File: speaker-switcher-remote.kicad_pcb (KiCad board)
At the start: 2 copper layers, 91 x 60 mm, 30 parts, among them M1 arduino-nano, Q1 2N2222, Q2 TIP31C, U1 LM7805_TO220

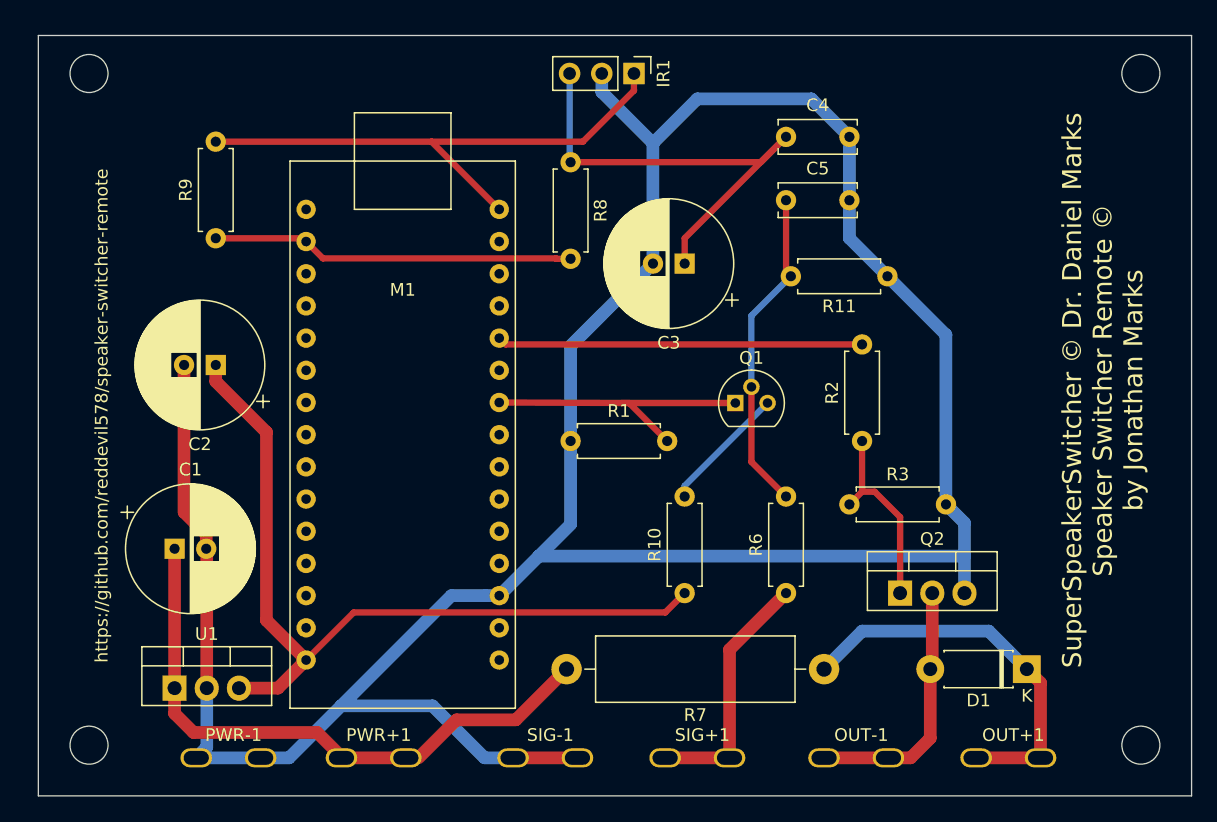
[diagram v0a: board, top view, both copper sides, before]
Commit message: Elongated board to required mounting width
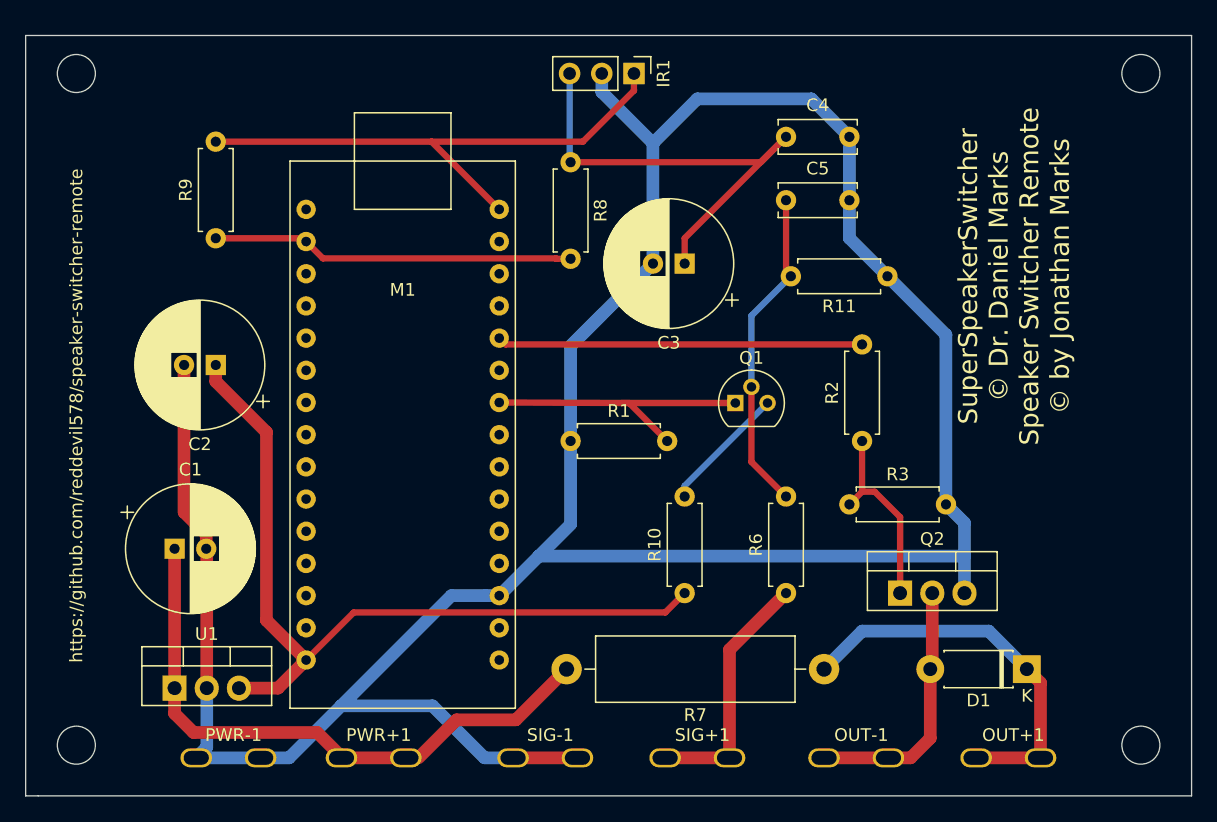
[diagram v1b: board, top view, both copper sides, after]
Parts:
- moved REF** 1.00 mm to (106.2, 71.5)
- moved REF** 1.00 mm to (106.2, 124.5)
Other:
- board size 91 x 60 mm -> 92 x 60 mm
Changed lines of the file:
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@@
   (general
     (thickness 1.6)
-    (drawings 6)
+    (drawings 7)
     (tracks 114)
     (zones 0)
@@
   )
   (module MountingHole:MountingHole_3mm (layer F.Cu)
-    (at 107.25 71.5)
+    (at 106.25 71.5)
     (descr "Mounting Hole 3mm, no annular")
     (tags "mounting hole 3mm no annular")
@@
   )
   (module MountingHole:MountingHole_3mm (layer F.Cu)
-    (at 107.25 124.5)
+    (at 106.25 124.5)
     (descr "Mounting Hole 3mm, no annular")
     (tags "mounting hole 3mm no annular")
@@
     )
   )
-  (gr_text https://github.com/reddevil578/speaker-switcher-remote (at 108.25 98.5 90) (layer F.SilkS)
+  (gr_line (start 102.25 68.5) (end 194.25 68.5) (layer Edge.Cuts) (width 0.05))
+  (gr_line (start 102.25 128.5) (end 103.25 128.5) (layer Edge.Cuts) (width 0.05))
+  (gr_text https://github.com/reddevil578/speaker-switcher-remote (at 106.25 98.5 90) (layer F.SilkS)
     (effects (font (size 1 1) (thickness 0.25)))
   )
-  (gr_text "SuperSpeakerSwitcher © Dr. Daniel Marks\nSpeaker Switcher Remote ©\nby Jonathan Marks" (at 187.25 96.5 90) (layer F.SilkS)
+  (gr_text "SuperSpeakerSwitcher\n© Dr. Daniel Marks\nSpeaker Switcher Remote\n© by Jonathan Marks" (at 180.25 87.5 90) (layer F.SilkS)
     (effects (font (size 1.5 1.5) (thickness 0.3)))
   )
-  (gr_line (start 103.25 128.5) (end 103.25 68.5) (layer Edge.Cuts) (width 0.05))
+  (gr_line (start 102.25 128.5) (end 102.25 68.5) (layer Edge.Cuts) (width 0.05))
   (gr_line (start 194.25 128.5) (end 103.25 128.5) (layer Edge.Cuts) (width 0.05))
   (gr_line (start 194.25 68.5) (end 194.25 128.5) (layer Edge.Cuts) (width 0.05))
-  (gr_line (start 103.25 68.5) (end 194.25 68.5) (layer Edge.Cuts) (width 0.05))
   (segment (start 116.33 120.21) (end 116.54 120) (width 1) (layer F.Cu) (net 1) (status 30))
   (segment (start 116.54 109.04) (end 116.5 109) (width 1) (layer F.Cu) (net 1) (status 30))
@@
   (segment (start 116.5 109) (end 116.5 107.86863) (width 1) (layer F.Cu) (net 1) (status 10))
   (segment (start 140.71 125.5) (end 145.79 125.5) (width 1) (layer F.Cu) (net 1) (status 30))
-  (segment (start 134.28 76.88) (end 139.62 82.22) (width 0.5) (layer F.Cu) (net 2) (status 20))
-  (segment (start 117.25 76.88) (end 134.28 76.88) (width 0.5) (layer F.Cu) (net 2) (status 10))
-  (segment (start 158.25 97.5) (end 149.25 97.5) (width 0.5) (layer F.Cu) (net 10) (status 10))
-  (segment (start 149.25 97.5) (end 139.62 97.46) (width 0.5) (layer F.Cu) (net 10) (status 20))
-  (segment (start 140.12 92.88) (end 139.62 92.38) (width 0.5) (layer F.Cu) (net 12) (status 30))
-  (segment (start 168.25 92.88) (end 140.12 92.88) (width 0.5) (layer F.Cu) (net 12) (status 30))
-  (segment (start 152.71 125.5) (end 157.79 125.5) (width 1) (layer F.Cu) (net 30) (status 30))
-  (segment (start 117.25 95.8) (end 121.25 99.8) (width 1) (layer F.Cu) (net 31))
-  (segment (start 117.25 94.5) (end 117.25 95.8) (width 1) (layer F.Cu) (net 31) (status 10))
-  (segment (start 121.25 114.65) (end 124.38 117.78) (width 1) (layer F.Cu) (net 31) (status 20))
-  (segment (start 121.25 99.8) (end 121.25 114.65) (width 1) (layer F.Cu) (net 31))
-  (segment (start 122.16 120) (end 124.38 117.78) (width 1) (layer F.Cu) (net 31) (status 20))
-  (segment (start 119.08 120) (end 122.16 120) (width 1) (layer F.Cu) (net 31) (status 10))
-  (segment (start 152.722001 114.027999) (end 154.25 112.5) (width 0.5) (layer F.Cu) (net 31) (status 20))
-  (segment (start 128.132001 114.027999) (end 152.722001 114.027999) (width 0.5) (layer F.Cu) (net 31))
-  (segment (start 124.38 117.78) (end 128.132001 114.027999) (width 0.5) (layer F.Cu) (net 31) (status 10))
-  (segment (start 114 109) (end 114 120) (width 1) (layer F.Cu) (net 32) (status 30))
-  (segment (start 114 120.0475) (end 114 120) (width 1) (layer B.Cu) (net 32) (status 30))
-  (segment (start 114 120) (end 114 120.0475) (width 1) (layer F.Cu) (net 32) (status 30))
-  (segment (start 133.25 125.5) (end 136.25 122.5) (width 1) (layer F.Cu) (net 32))
-  (segment (start 140.93 122.5) (end 144.93 118.5) (width 1) (layer F.Cu) (net 32) (status 20))
-  (segment (start 136.25 122.5) (end 140.93 122.5) (width 1) (layer F.Cu) (net 32))
   (segment (start 176.33 112.5) (end 176.33 112.5475) (width 1) (layer B.Cu) (net 1) (status 30))
   (segment (start 145.25 93) (end 151.75 86.5) (width 1) (layer B.Cu) (net 1) (status 20))
@@
   (segment (start 123.04 125.5) (end 127.145 121.395) (width 1) (layer B.Cu) (net 1))
   (segment (start 127.145 121.395) (end 135.84 112.7) (width 1) (layer B.Cu) (net 1))
+  (segment (start 134.28 76.88) (end 139.62 82.22) (width 0.5) (layer F.Cu) (net 2) (status 20))
+  (segment (start 117.25 76.88) (end 134.28 76.88) (width 0.5) (layer F.Cu) (net 2) (status 10))
+  (segment (start 150.25 71.5) (end 150.33 71.5) (width 0.5) (layer F.Cu) (net 2) (status 30))
+  (segment (start 150.25 71.5) (end 150.25 71.032002) (width 0.5) (layer F.Cu) (net 2))
+  (segment (start 150.25 72.85) (end 150.25 71.5) (width 0.5) (layer F.Cu) (net 2))
+  (segment (start 146.22 76.88) (end 150.25 72.85) (width 0.5) (layer F.Cu) (net 2))
+  (segment (start 134.28 76.88) (end 146.22 76.88) (width 0.5) (layer F.Cu) (net 2))
+  (segment (start 158.25 97.5) (end 149.25 97.5) (width 0.5) (layer F.Cu) (net 10) (status 10))
+  (segment (start 149.25 97.5) (end 139.62 97.46) (width 0.5) (layer F.Cu) (net 10) (status 20))
   (segment (start 149.87 97.5) (end 149.25 97.5) (width 0.5) (layer F.Cu) (net 10))
   (segment (start 152.87 100.5) (end 149.87 97.5) (width 0.5) (layer F.Cu) (net 10) (status 10))
+  (segment (start 140.12 92.88) (end 139.62 92.38) (width 0.5) (layer F.Cu) (net 12) (status 30))
+  (segment (start 168.25 92.88) (end 140.12 92.88) (width 0.5) (layer F.Cu) (net 12) (status 30))
   (segment (start 168.25 104.5) (end 167.25 105.5) (width 0.5) (layer F.Cu) (net 29) (status 20))
   (segment (start 168.25 100.5) (end 168.25 104.5) (width 0.5) (layer F.Cu) (net 29) (status 10))
@@
   (segment (start 171.25 106.5) (end 171.25 112.5) (width 0.5) (layer F.Cu) (net 29) (status 20))
   (segment (start 169.25 104.5) (end 171.25 106.5) (width 0.5) (layer F.Cu) (net 29))
+  (segment (start 152.71 125.5) (end 157.79 125.5) (width 1) (layer F.Cu) (net 30) (status 30))
   (segment (start 157.79 116.96) (end 157.79 125.5) (width 1) (layer F.Cu) (net 30) (status 20))
   (segment (start 162.25 112.5) (end 157.79 116.96) (width 1) (layer F.Cu) (net 30) (status 10))
-  (segment (start 150.25 71.5) (end 150.33 71.5) (width 0.5) (layer F.Cu) (net 2) (status 30))
-  (segment (start 150.25 71.5) (end 150.25 71.032002) (width 0.5) (layer F.Cu) (net 2))
-  (segment (start 150.25 72.85) (end 150.25 71.5) (width 0.5) (layer F.Cu) (net 2))
-  (segment (start 146.22 76.88) (end 150.25 72.85) (width 0.5) (layer F.Cu) (net 2))
-  (segment (start 134.28 76.88) (end 146.22 76.88) (width 0.5) (layer F.Cu) (net 2))
+  (segment (start 117.25 95.8) (end 121.25 99.8) (width 1) (layer F.Cu) (net 31))
+  (segment (start 117.25 94.5) (end 117.25 95.8) (width 1) (layer F.Cu) (net 31) (status 10))
+  (segment (start 121.25 114.65) (end 124.38 117.78) (width 1) (layer F.Cu) (net 31) (status 20))
+  (segment (start 121.25 99.8) (end 121.25 114.65) (width 1) (layer F.Cu) (net 31))
+  (segment (start 122.16 120) (end 124.38 117.78) (width 1) (layer F.Cu) (net 31) (status 20))
+  (segment (start 119.08 120) (end 122.16 120) (width 1) (layer F.Cu) (net 31) (status 10))
+  (segment (start 152.722001 114.027999) (end 154.25 112.5) (width 0.5) (layer F.Cu) (net 31) (status 20))
+  (segment (start 128.132001 114.027999) (end 152.722001 114.027999) (width 0.5) (layer F.Cu) (net 31))
+  (segment (start 124.38 117.78) (end 128.132001 114.027999) (width 0.5) (layer F.Cu) (net 31) (status 10))
+  (segment (start 114 109) (end 114 120) (width 1) (layer F.Cu) (net 32) (status 30))
+  (segment (start 114 120.0475) (end 114 120) (width 1) (layer B.Cu) (net 32) (status 30))
+  (segment (start 114 120) (end 114 120.0475) (width 1) (layer F.Cu) (net 32) (status 30))
+  (segment (start 133.25 125.5) (end 136.25 122.5) (width 1) (layer F.Cu) (net 32))
+  (segment (start 140.93 122.5) (end 144.93 118.5) (width 1) (layer F.Cu) (net 32) (status 20))
+  (segment (start 136.25 122.5) (end 140.93 122.5) (width 1) (layer F.Cu) (net 32))
   (segment (start 114 122) (end 115.5 123.5) (width 1) (layer F.Cu) (net 32))
   (segment (start 114 120) (end 114 122) (width 1) (layer F.Cu) (net 32))
@@
     (polygon
       (pts
-        (xy 105.25 128.5) (xy 103.25 128.5) (xy 103.25 68.5) (xy 105.25 68.5)
+        (xy 104.25 128.5) (xy 102.25 128.5) (xy 102.25 68.5) (xy 104.25 68.5)
       )
     )

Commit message: Updated board as per Dan's remarks
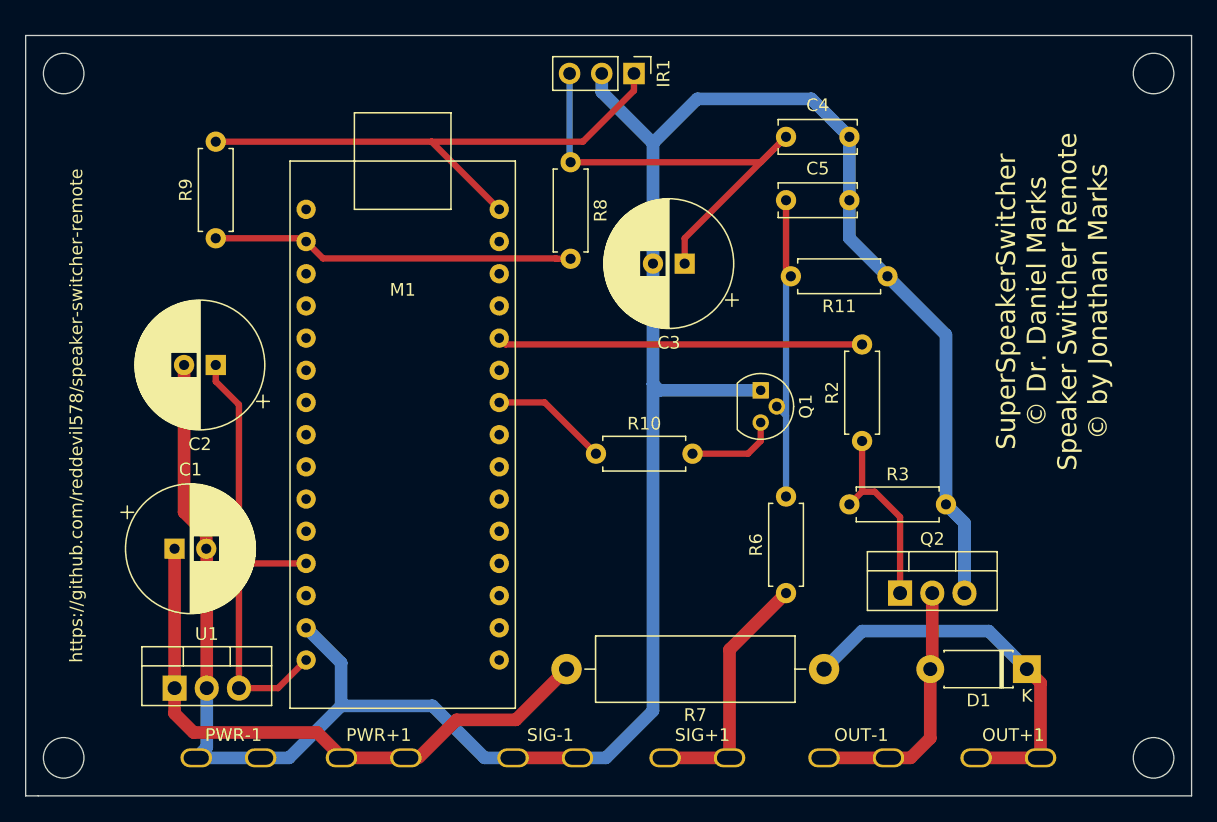
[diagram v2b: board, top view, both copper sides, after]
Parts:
- removed R1: 100k, Resistor_THT:R_Axial_DIN0207_L6.3mm_D2.5mm_P7.62mm_Horizontal
- removed the REF** at (190.2, 71.5)
- removed the REF** at (106.2, 71.5)
- removed the REF** at (106.2, 124.5)
- removed the REF** at (190.2, 124.5)
- added REF**: MountingHole_3.2mm_M3, MountingHole:MountingHole_3.2mm_M3, F.Cu at (105.2, 125.5)
- added REF**: MountingHole_3.2mm_M3, MountingHole:MountingHole_3.2mm_M3, F.Cu at (191.2, 125.5)
- added REF**: MountingHole_3.2mm_M3, MountingHole:MountingHole_3.2mm_M3, F.Cu at (191.2, 71.5)
- added REF**: MountingHole_3.2mm_M3, MountingHole:MountingHole_3.2mm_M3, F.Cu at (105.2, 71.5)
- R10: value 100 -> 10k
- moved R10 13.0 mm to (147.2, 101.5), turned to 0 degrees
- moved Q1 2.24 mm to (160.2, 96.5), turned to 270 degrees
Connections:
- C2 pad 1: +5V -> /+5V
- M1 pad 12: Net-(M1-Pad12) -> /+5V
- M1 pad 14: Net-(M1-Pad14) -> GNDREF
- M1 pad 15: +5V -> /+5V
- M1 pad 28: GNDREF -> Net-(M1-Pad28)
- Q1 pad 1: Net-(M1-Pad22) -> GNDREF
- R10 pad 1: +5V -> Net-(M1-Pad22)
- U1 pad 3: +5V -> /+5V
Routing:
- net +5V: track 64.5 -> 0.00 mm
- net /+5V: track 0.00 -> 37.8 mm
- net GNDREF: track 224.9 -> 199.3 mm
- net Net-(M1-Pad22): track 23.5 -> 9.30 mm
- net Net-(Q1-Pad3): track 10.1 -> 7.25 mm
- net Net-(C5-Pad1): track 26.0 -> 25.2 mm

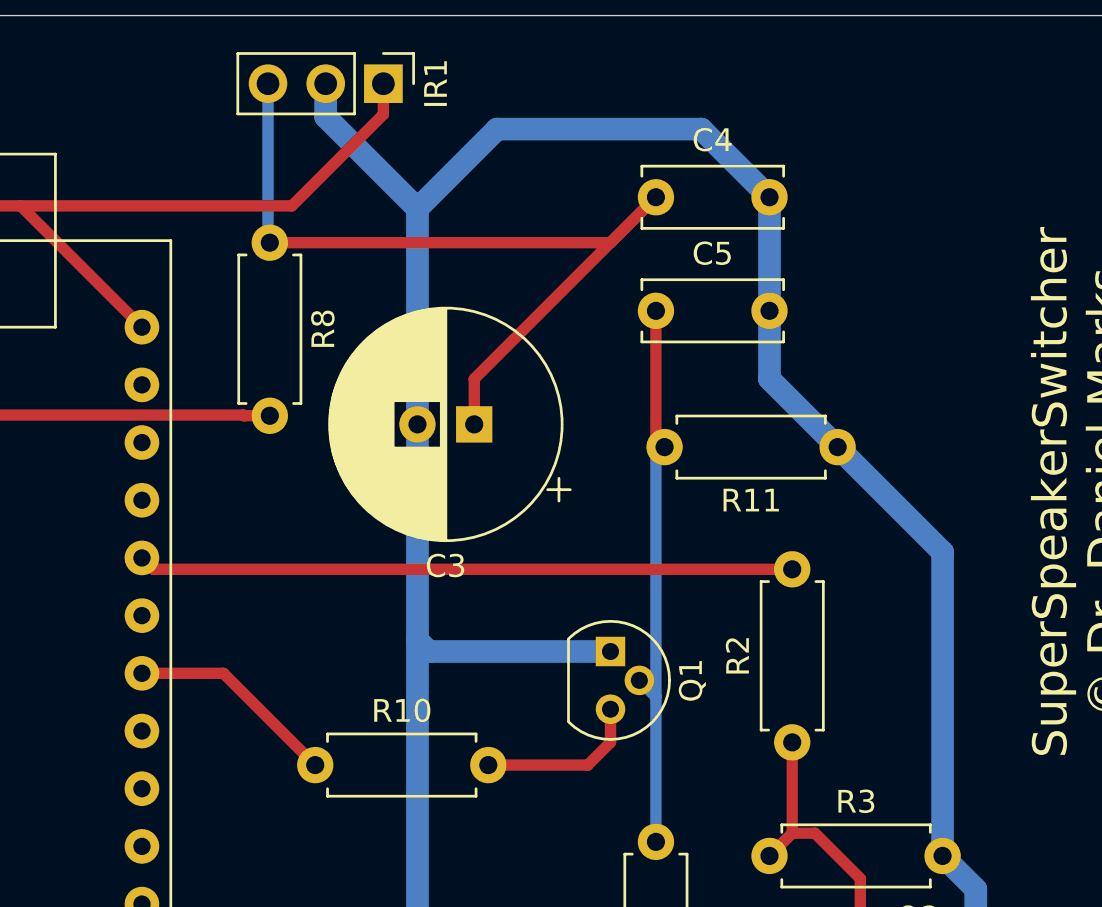
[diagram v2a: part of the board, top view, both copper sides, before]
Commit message: Added indicator LED to d09
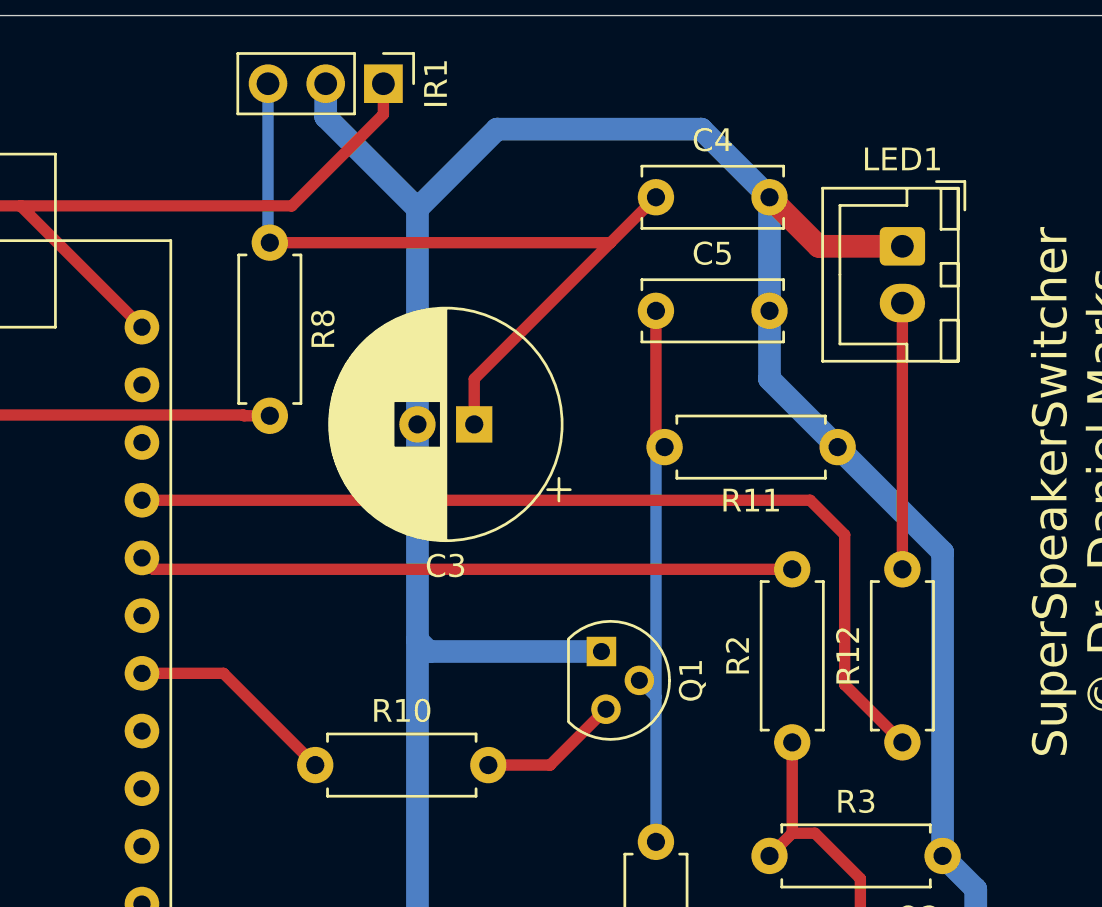
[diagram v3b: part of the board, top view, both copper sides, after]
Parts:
- added LED1: LED, Connector_JST:JST_XH_B2B-XH-A_1x02_P2.50mm_Vertical, F.Cu at (173.1, 78.7)
- added R12: 150, Resistor_THT:R_Axial_DIN0207_L6.3mm_D2.5mm_P7.62mm_Horizontal, F.Cu at (173.1, 100.5)
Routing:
- net Net-(M1-Pad19): track 0.00 -> 41.8 mm
- net Net-(LED1-Pad2): track 0.00 -> 11.7 mm
- net GNDREF: track 199.3 -> 205.7 mm
- net Net-(C3-Pad1): track 38.3 -> 35.5 mm
- net Net-(Q1-Pad3): track 7.25 -> 6.20 mm
